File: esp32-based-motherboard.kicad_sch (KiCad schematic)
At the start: 69 parts, among them J3 USB_C_Receptacle_USB2.0_16P, J4 USB_A, J5 USB_C_Receptacle_USB2.0_16P, J6 USB_C_Receptacle_USB2.0_16P, J7 Conn_01x03_Pin, J8 Conn_01x03_Pin, SW1 SW_Push, SW2 SW_Push, SW3 SW_Push, SW4 SW_Push, SW5 SW_SPST, U12 CP2102N-Axx-xQFN24, U4 ESP32-P4_MODULE, U6 ADM3053

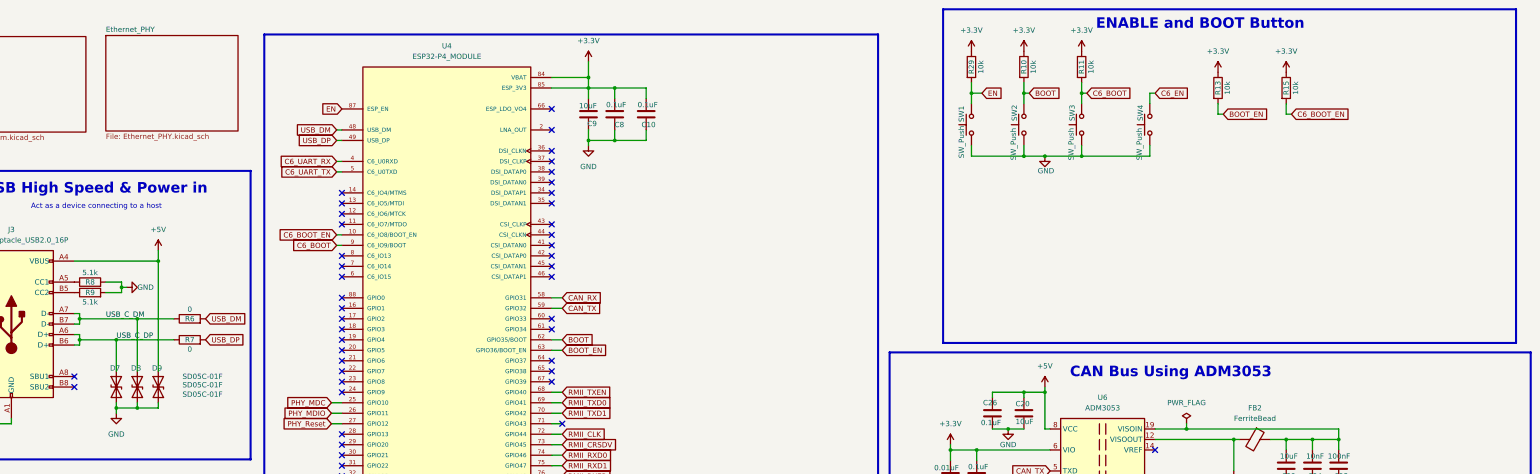
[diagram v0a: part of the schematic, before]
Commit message: ESP32 P4 with 8 Ethernet
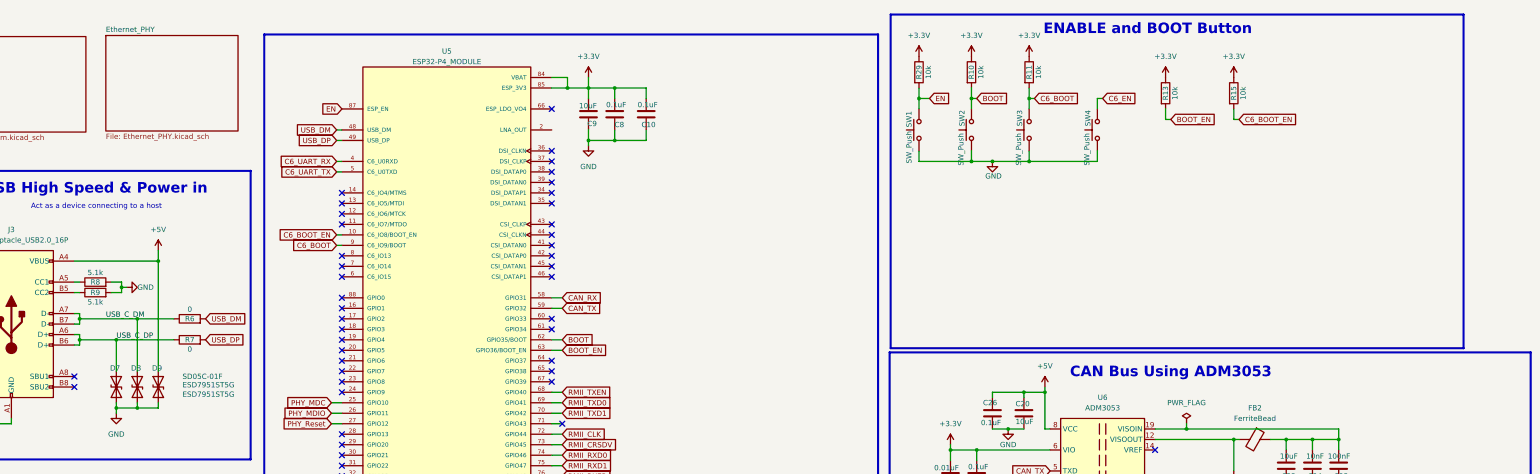
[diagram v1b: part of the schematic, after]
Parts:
- removed U4: ESP32-P4_MODULE, ESP32-P4:XCVR_ESP32-P4_MODULE, symbol ESP32-P4_MODULE:ESP32-P4_MODULE
- added U5: ESP32-P4_MODULE, Custom_Footprint:ESP32-P4_MODULE, symbol ESP32-P4_MODULE:ESP32-P4_MODULE
- D16, D17: footprint (none) -> LED_SMD:LED_0603_1608Metric
- D7, D8: value SD05C-01F -> ESD7951ST5G
- FB1, FB2: footprint (none) -> Inductor_SMD:L_0603_1608Metric
- J3, J5, J6: footprint (none) -> Connector_USB:USB_C_Receptacle_Palconn_UTC16-G
- J4: footprint (none) -> Connector_USB:USB_A_Molex_67643_Horizontal
- J7, J8: footprint (none) -> Connector_JST:JST_PH_B3B-PH-K_1x03_P2.00mm_Vertical
- R10, R11, R12, R13, R14, R15, R17, R18, R19, R20, R21, R23, R24, R25, R29, R31, R4, R5, R6, R7, R8, R9: footprint (none) -> Resistor_SMD:R_0603_1608Metric
- SW5: footprint (none) -> Custom_Footprint:DSIC01LHGET_C54957
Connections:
- net +3.3V: now also U5.84 (VBAT), U5.85 (ESP_3V3), U5.86 (ESP_3V3)
- net BOOT: now also U5.62 (GPIO35/BOOT)
- net BOOT_EN: now also U5.63 (GPIO36/BOOT_EN)
- net C6_BOOT: now also U5.9 (C6_IO9/BOOT)
- net C6_BOOT_EN: now also U5.10 (C6_IO8/BOOT_EN)
- net C6_EN: now also U5.82 (GPIO54)
- net C6_UART_RX: now also U5.4 (C6_U0RXD)
- net C6_UART_TX: now also U5.5 (C6_U0TXD)
- net CAN_RX: now also U5.58 (GPIO31)
- net CAN_TX: now also U5.59 (GPIO32)
- net EN: now also U5.87 (ESP_EN)
- net GND: now also U5.1 (GND), U5.15 (GND), U5.3 (GND), U5.33 (GND), U5.40 (GND), U5.47 (GND), U5.52 (GND), U5.83 (GND)
- net PHY_MDC: now also U5.25 (GPIO10)
- net PHY_MDIO: now also U5.26 (GPIO11)
- net PHY_Reset: now also U5.27 (GPIO12)
- net RMII_CLK: now also U5.72 (GPIO44)
- net RMII_CRSDV: now also U5.73 (GPIO45)
- net RMII_RXD0: now also U5.74 (GPIO46)
- net RMII_RXD1: now also U5.75 (GPIO47)
- net RMII_RXER: now also U5.76 (GPIO48)
- net RMII_TXD0: now also U5.69 (GPIO41)
- net RMII_TXD1: now also U5.70 (GPIO42)
- net RMII_TXEN: now also U5.68 (GPIO40)
- net USB1P1_N: now also U5.50 (GPIO24/USB1P1_N0)
- net USB1P1_P: now also U5.51 (GPIO25/USB1P1_P0)
- net USB_DM: now also U5.48 (USB_DM)
- net USB_DP: now also U5.49 (USB_DP)
- no-connect marks 69 -> 68
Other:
- moved on the sheet: R10, R11, R13, R15, R29, R8, R9, SW1, SW2, SW3, SW4
